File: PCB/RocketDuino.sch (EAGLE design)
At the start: 40 parts, among them J1 FTDI, Y1 16MHZ

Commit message: Add control for the Charges.  Whoops. (2)
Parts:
- added FRAME1: FRAME-LEDGER, SparkFun-Aesthetics:FRAME-LEDGER
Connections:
- net CHARGE1: now also ATMEGA2560AU.PJ6(PCINT15)
- net CHARGE2: now also ATMEGA2560AU.PJ5(PCINT14)
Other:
- note added: "0.1"
- note added: "Joshua Villwock"
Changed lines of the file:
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@@
 <part name="GND14" library="SparkFun-Aesthetics" deviceset="GND" device=""/>
 <part name="TX/RX" library="SparkFun-Connectors" deviceset="M06" device="SILK_FEMALE_PTH"/>
+<part name="FRAME1" library="SparkFun-Aesthetics" deviceset="FRAME-LEDGER" device=""/>
 </parts>
 <sheets>
@@
 <wire x1="294.64" y1="162.56" x2="294.64" y2="99.06" width="0.1524" layer="105"/>
 <text x="215.9" y="160.02" size="1.778" layer="105">LEDs</text>
-<text x="139.954" y="40.894" size="1.27" layer="105">(LED)</text>
+<text x="137.414" y="40.894" size="1.27" layer="105">(LED)</text>
 <wire x1="213.36" y1="223.52" x2="294.64" y2="223.52" width="0.1524" layer="105"/>
 <wire x1="294.64" y1="223.52" x2="294.64" y2="167.64" width="0.1524" layer="105"/>
@@
 <text x="231.14" y="139.7" size="1.778" layer="97">blue</text>
 <text x="231.14" y="152.4" size="1.778" layer="97">red</text>
+<text x="299.72" y="-35.56" size="5.08" layer="97">Joshua Villwock</text>
+<text x="368.554" y="-36.83" size="3.81" layer="97">0.1</text>
 </plain>
 <instances>
@@
 <instance part="GND14" gate="1" x="259.08" y="71.12"/>
 <instance part="TX/RX" gate="G$1" x="17.78" y="167.64"/>
+<instance part="FRAME1" gate="G$1" x="-50.8" y="-43.18"/>
+<instance part="FRAME1" gate="G$2" x="279.4" y="-43.18"/>
 </instances>
 <busses>
@@
 <pinref part="C4" gate="G$1" pin="1"/>
 <pinref part="C3" gate="G$1" pin="1"/>
-<label x="136.398" y="40.64" size="1.778" layer="95"/>
+<label x="133.858" y="40.64" size="1.778" layer="95"/>
 <pinref part="VREG" gate="G$1" pin="OUT"/>
-<wire x1="124.46" y1="40.64" x2="144.78" y2="40.64" width="0.1524" layer="91"/>
+<wire x1="124.46" y1="40.64" x2="142.24" y2="40.64" width="0.1524" layer="91"/>
 <wire x1="71.12" y1="40.64" x2="76.2" y2="40.64" width="0.1524" layer="91"/>
 <pinref part="VREG" gate="G$1" pin="OUT@1"/>
@@
 <junction x="241.3" y="182.88"/>
 </segment>
+<segment>
+<pinref part="ATMEGA2560AU" gate="1" pin="PJ5(PCINT14)"/>
+<wire x1="109.22" y1="101.6" x2="96.52" y2="101.6" width="0.1524" layer="91"/>
+<label x="96.52" y="101.6" size="1.778" layer="95"/>
+</segment>
 </net>
 <net name="CHARGE1" class="0">
@@
 <junction x="241.3" y="203.2"/>
 </segment>
-</net>
+<segment>
+<pinref part="ATMEGA2560AU" gate="1" pin="PJ6(PCINT15)"/>
+<wire x1="109.22" y1="104.14" x2="96.52" y2="104.14" width="0.1524" layer="91"/>
+<label x="96.52" y="104.14" size="1.778" layer="95"/>
+</segment>
+</net>

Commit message: Organize the Schematic Nicely
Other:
- note added: "0.4"
- note added: "RocketDuino v0.4"
- note removed: "0.1"
- moved on the sheet: 13, C5, C6, CH_1, CH_2, D1, GPS, I2C, ICSP, J1, MOS1, MOS2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

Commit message: Clean schematic; Shift Board componets 2
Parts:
- removed D2: (no value), SparkFun-DiscreteSemi:DIODESMA-ALT
- removed P_L: (no value), led:LEDSML0805
- added C8: 10uF, SparkFun-Capacitors:CAP1206
- added MAIN, MOS: (no value), SparkFun-Connectors:M02LOCK_LONGPADS
- POWER: device SparkFun-Connectors:M02LOCK_LONGPADS -> led:LEDSML0805
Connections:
- removed net VIN_RECTIFIED: C1.1, C2.1, D2.C, R4.1, VREG.IN
- new net VIN_MOS: CH_1.2, CH_2.2, MOS.1
- net 5V: now also C8.1
- net GND: now also C8.2, MAIN.2, MOS.2, POWER.C; no longer POWER.1, P_L.C
- net N$2: now also POWER.A; no longer P_L.A
- net VIN: now also C1.1, C2.1, MAIN.1, R4.1, VREG.IN; no longer CH_1.2, CH_2.2, D2.A, POWER.2
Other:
- moved on the sheet: 13, ATMEGA2560AU, C10, C5, C6, CH_1, CH_2, D1, GPS, I2C, ICSP, J1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

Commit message: tired
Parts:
- removed TX/RX: (no value), SparkFun-Connectors:M06SILK_FEMALE_PTH
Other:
- moved on the sheet: C5, C6, C8, D1, ICSP, J1, R2, SW_RESET

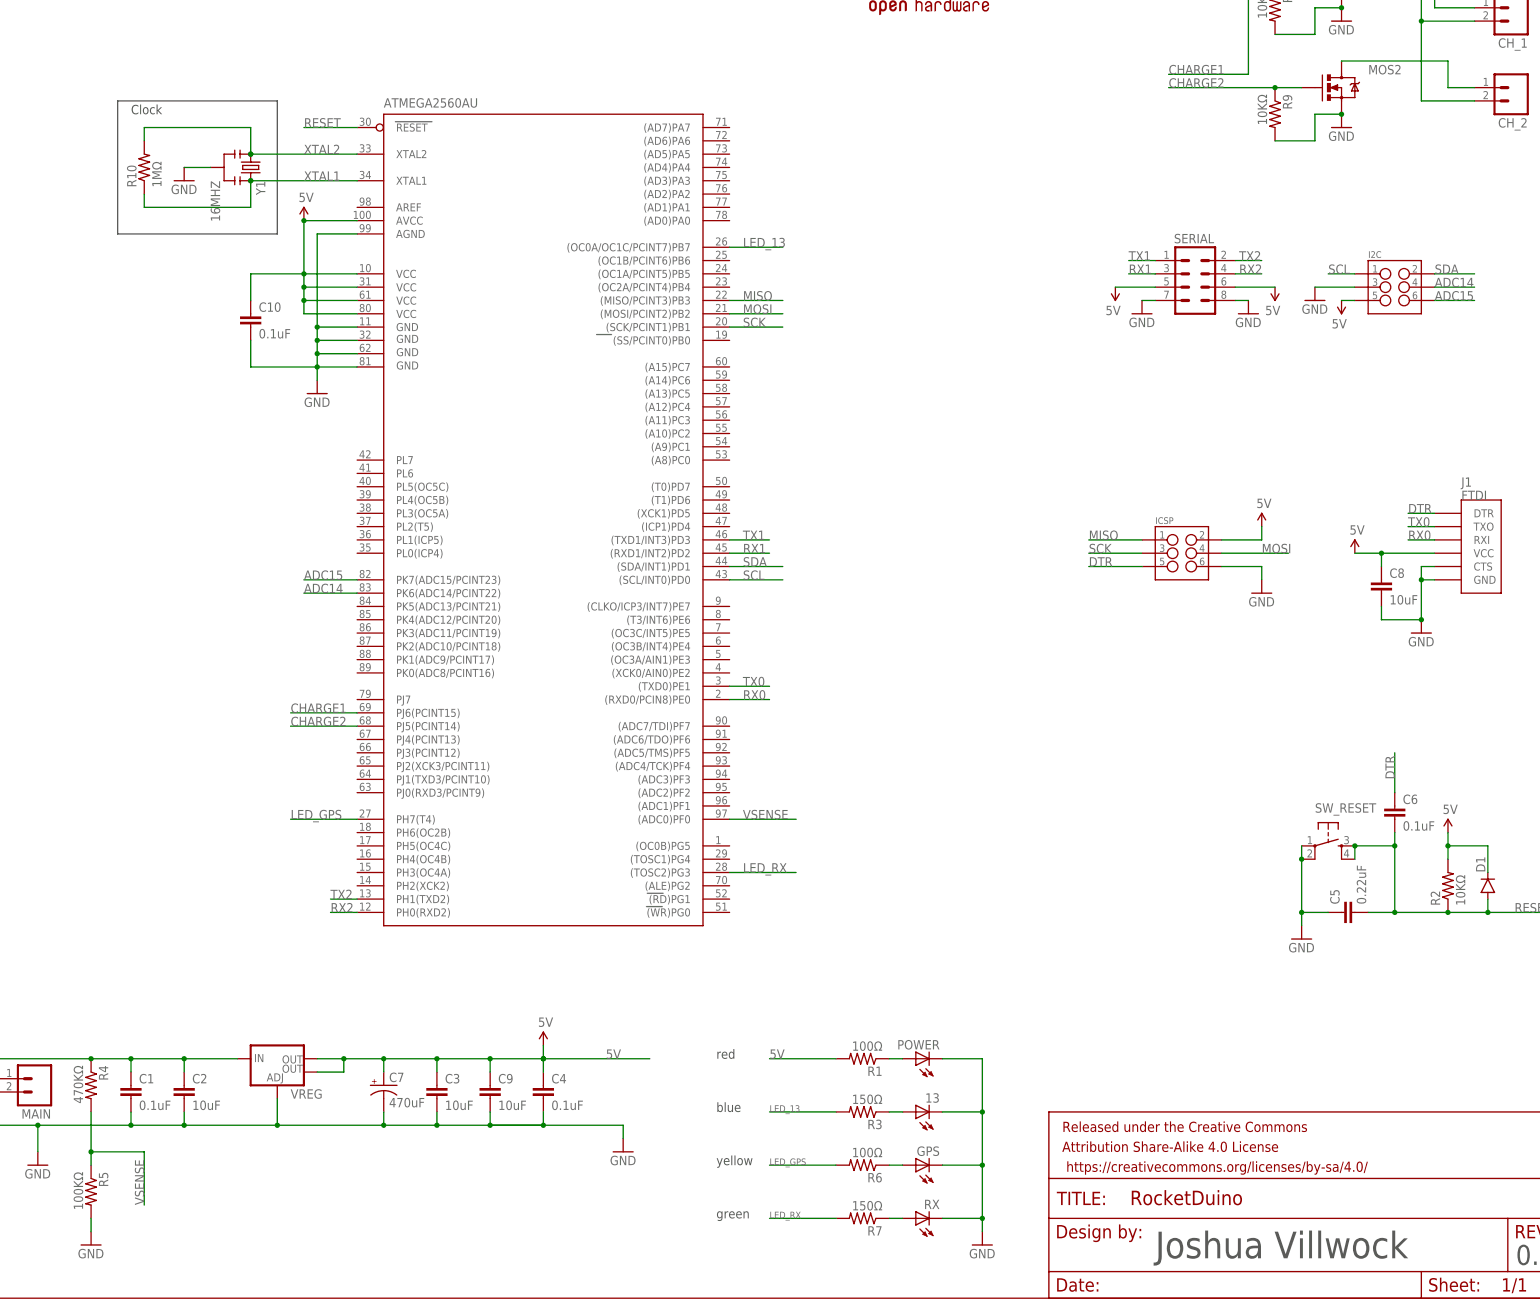
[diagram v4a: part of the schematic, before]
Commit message: Clean up all Silkscreen Indicators
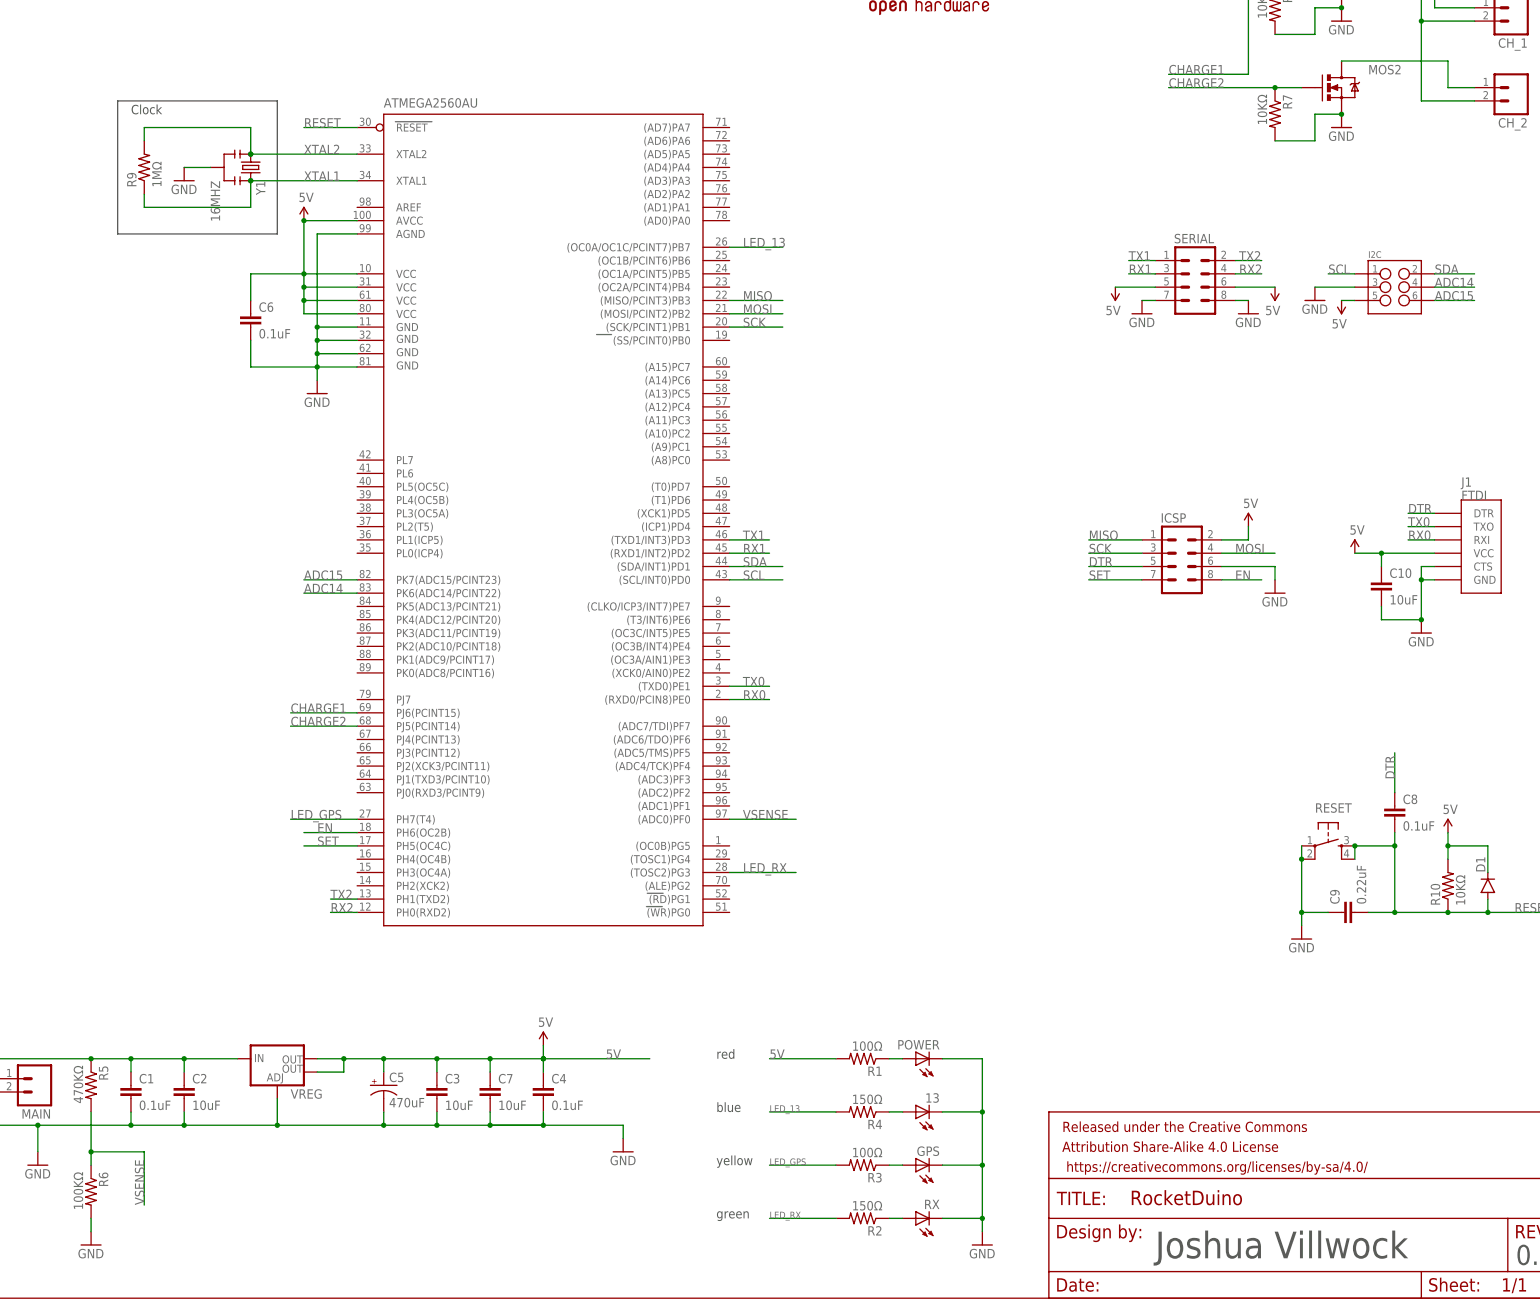
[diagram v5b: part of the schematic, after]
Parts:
- C10: value 0.1uF -> 10uF
- C5: value 0.22uF -> 470uF; device SparkFun-Capacitors:CAP1206 -> SparkFun-Capacitors:CAP_POLPTH1
- C7: value 470uF -> 10uF; device SparkFun-Capacitors:CAP_POLPTH1 -> SparkFun-Capacitors:CAP1206
- C8: value 10uF -> 0.1uF
- C9: value 10uF -> 0.22uF
- ICSP: device SparkFun-Connectors:M03X2FEMALE_SMD -> SparkFun-Connectors:M04X2
- R10: value 1MΩ -> 10KΩ
- R2: value 10KΩ -> 150Ω
- R3: value 150Ω -> 100Ω
- R4: value 470KΩ -> 150Ω
- R5: value 100KΩ -> 470KΩ
- R6: value 100Ω -> 100KΩ
- R7: value 150Ω -> 10KΩ
- R9: value 10KΩ -> 1MΩ
- renumbered SW_RESET to RESET
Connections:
- new net EN: ATMEGA2560AU.PH6(OC2B), ICSP.8
- new net SET: ATMEGA2560AU.PH5(OC4C), ICSP.7
- net 5V: now also C5.+, C6.1, C7.1, R10.2; no longer C7.+, C8.1, C9.1, R2.2
- net CHARGE2: now also R7.1; no longer R9.1
- net DTR: now also C8.1; no longer C6.1
- net GND: now also C5.-, C6.2, C7.2, C9.1, R6.2, R7.2; no longer C5.1, C7.-, C8.2, C9.2, R5.2, R9.2
- net LED_13: now also R4.2; no longer R3.2
- net LED_GPS: now also R3.2; no longer R6.2
- net LED_RX: now also R2.2; no longer R7.2
- net N$1: now also R3.1; no longer R6.1
- net N$3: now also R4.1; no longer R3.1
- net N$4: now also R2.1; no longer R7.1
- net RESET: now also C8.2, C9.2, R10.1; no longer C5.2, C6.2, R2.1
- net VIN: now also R5.1; no longer R4.1
- net VSENSE: now also R5.2, R6.1; no longer R4.2, R5.1
- net XTAL1: now also R9.1; no longer R10.1
- net XTAL2: now also R9.2; no longer R10.2
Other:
- moved on the sheet: C10, C6, C8, C9, R10, R2, R3, R4, R5, R6, R7, R9
